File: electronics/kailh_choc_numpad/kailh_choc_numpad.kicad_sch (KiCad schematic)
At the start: 135 parts, among them J1 Conn_01x06, U1 PCA9554, U2 PCA9535

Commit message: updated broken IC footprint, added OHW logo
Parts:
- added N2: OHWLOGO, Symbol:OSHW-Symbol_8.9x8mm_SilkScreen, symbol SquantorLabels:OHWLOGO
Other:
- moved on the sheet: N1
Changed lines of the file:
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@@
     (stroke (width 0) (type default) (color 0 0 0 0))
   )
-  (polyline (pts (xy 175.26 185.42) (xy 157.48 185.42))
+  (polyline (pts (xy 175.26 173.99) (xy 157.48 173.99))
     (stroke (width 0) (type default) (color 0 0 0 0))
   )
@@
     (stroke (width 0) (type default) (color 0 0 0 0))
   )
-  (polyline (pts (xy 157.48 185.42) (xy 157.48 196.85))
+  (polyline (pts (xy 157.48 173.99) (xy 157.48 196.85))
     (stroke (width 0) (type default) (color 0 0 0 0))
   )
@@
     (stroke (width 0) (type default) (color 0 0 0 0))
   )
-  (polyline (pts (xy 175.26 196.85) (xy 175.26 185.42))
+  (polyline (pts (xy 175.26 196.85) (xy 175.26 173.99))
     (stroke (width 0) (type default) (color 0 0 0 0))
   )
@@
     (pin "2")
   )
+  (symbol (lib_id "SquantorLabels:OHWLOGO") (at 166.37 186.69 0) (unit 1)
+    (in_bom yes) (on_board yes)
+    (property "Reference" "N2" (id 0) (at 165.1 182.88 0)
+      (effects (font (size 1.524 1.524)) (justify left))
+    )
+    (property "Value" "OHWLOGO" (id 1) (at 161.29 190.5 0)
+      (effects (font (size 1.524 1.524)) (justify left))
+    )
+    (property "Footprint" "Symbol:OSHW-Symbol_8.9x8mm_SilkScreen" (id 2) (at 166.37 186.69 0)
+      (effects (font (size 1.524 1.524)) hide)
+    )
+    (property "Datasheet" "" (id 3) (at 166.37 186.69 0)
+      (effects (font (size 1.524 1.524)) hide)
+    )
+  )
   (symbol (lib_id "power:VDD") (at 43.18 41.91 270) (unit 1)
     (in_bom yes) (on_board yes)
@@
     )
   )
-  (symbol (lib_id "SquantorLabels:VYYYYMMDD") (at 166.37 190.5 0) (unit 1)
+  (symbol (lib_id "SquantorLabels:VYYYYMMDD") (at 166.37 179.07 0) (unit 1)
     (in_bom yes) (on_board yes)
-    (property "Reference" "N1" (id 0) (at 165.1 187.96 0)
+    (property "Reference" "N1" (id 0) (at 165.1 176.53 0)
       (effects (font (size 1.524 1.524)) (justify left))
     )
-    (property "Value" "V20220626" (id 1) (at 160.02 190.5 0)
+    (property "Value" "V20220626" (id 1) (at 160.02 179.07 0)
       (effects (font (size 1.524 1.524)) (justify left))
     )
-    (property "Footprint" "SquantorLabels:Label_Generic" (id 2) (at 166.37 190.5 0)
+    (property "Footprint" "SquantorLabels:Label_Generic" (id 2) (at 166.37 179.07 0)
       (effects (font (size 1.524 1.524)) hide)
     )
-    (property "Datasheet" "" (id 3) (at 166.37 190.5 0)
+    (property "Datasheet" "" (id 3) (at 166.37 179.07 0)
       (effects (font (size 1.524 1.524)) hide)
     )
@@
       (reference "N1") (unit 1) (value "V20220626") (footprint "SquantorLabels:Label_Generic")
     )
+    (path "/8a622108-1bf1-4789-8ead-8e70429237d1"
+      (reference "N2") (unit 1) (value "OHWLOGO") (footprint "Symbol:OSHW-Symbol_8.9x8mm_SilkScreen")
+    )
     (path "/69128f69-413a-42fa-86a0-bccc9ea098f6"

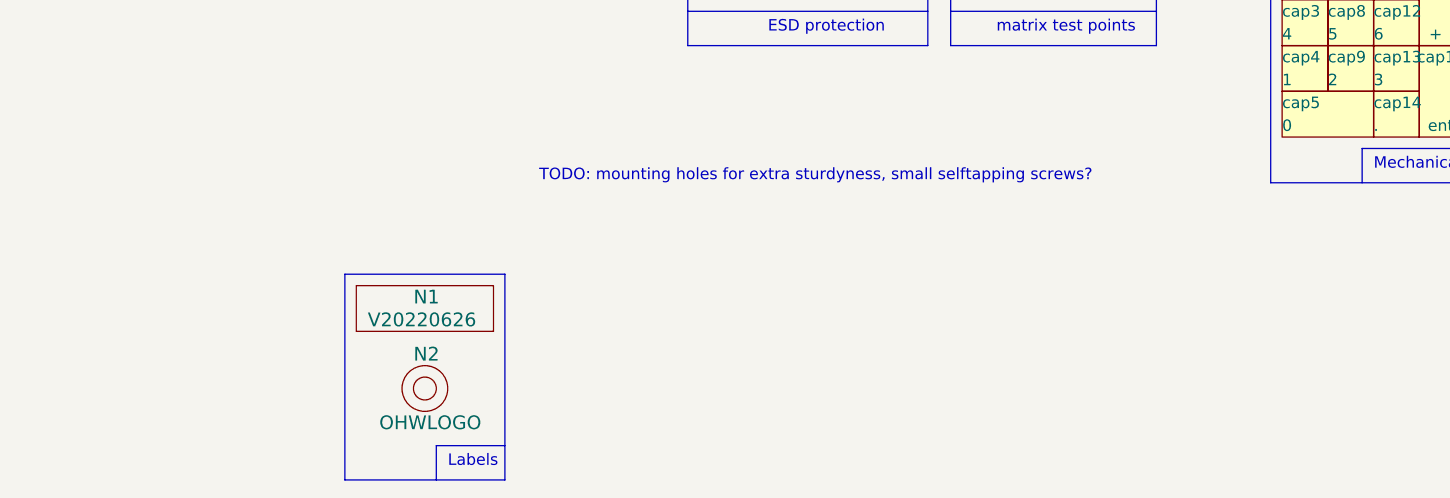
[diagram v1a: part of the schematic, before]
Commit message: added mounting holes
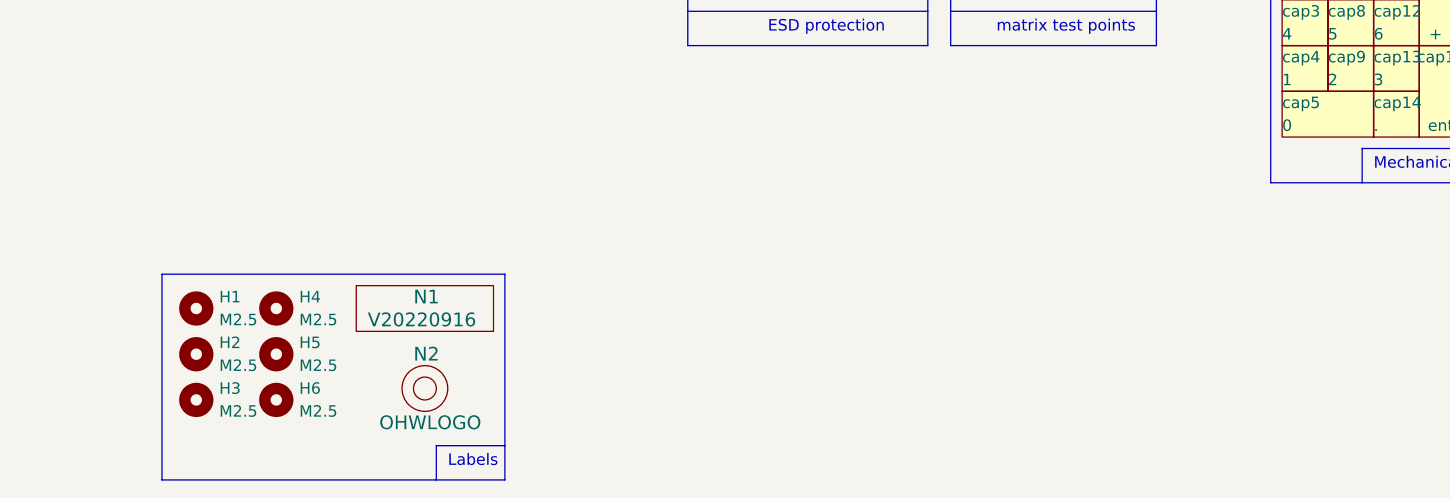
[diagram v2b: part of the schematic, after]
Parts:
- added H1, H2, H3, H4, H5, H6: M2.5, MountingHole:MountingHole_2.7mm_M2.5, symbol Mechanical:MountingHole
- N1: value V20220626 -> V20220916
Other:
- note removed: "TODO: mounting holes for extra sturdyness, small selftapping screws?"
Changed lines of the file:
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@@
     (stroke (width 0) (type default) (color 0 0 0 0))
   )
-  (polyline (pts (xy 175.26 173.99) (xy 157.48 173.99))
+  (polyline (pts (xy 175.26 173.99) (xy 137.16 173.99))
     (stroke (width 0) (type default) (color 0 0 0 0))
   )
@@
     (stroke (width 0) (type default) (color 0 0 0 0))
   )
-  (polyline (pts (xy 157.48 173.99) (xy 157.48 196.85))
+  (polyline (pts (xy 137.16 173.99) (xy 137.16 196.85))
     (stroke (width 0) (type default) (color 0 0 0 0))
   )
@@
     (stroke (width 0) (type default) (color 0 0 0 0))
   )
-  (polyline (pts (xy 157.48 196.85) (xy 175.26 196.85))
+  (polyline (pts (xy 137.16 196.85) (xy 175.26 196.85))
     (stroke (width 0) (type default) (color 0 0 0 0))
   )
@@
     (effects (font (size 1.27 1.27)) (justify left bottom))
   )
-  (text "TODO: mounting holes for extra sturdyness, small selftapping screws?"
-    (at 179.07 163.83 0)
-    (effects (font (size 1.27 1.27)) (justify left bottom))
-  )
   (text "matrix test points" (at 229.87 147.32 0)
     (effects (font (size 1.27 1.27)) (justify left bottom))
@@
     (pin "2")
   )
+  (symbol (lib_id "Mechanical:MountingHole") (at 140.97 177.8 0) (unit 1)
+    (in_bom yes) (on_board yes)
+    (property "Reference" "H1" (id 0) (at 143.51 176.53 0)
+      (effects (font (size 1.27 1.27)) (justify left))
+    )
+    (property "Value" "M2.5" (id 1) (at 143.51 179.07 0)
+      (effects (font (size 1.27 1.27)) (justify left))
+    )
+    (property "Footprint" "MountingHole:MountingHole_2.7mm_M2.5" (id 2) (at 140.97 177.8 0)
+      (effects (font (size 1.27 1.27)) hide)
+    )
+    (property "Datasheet" "~" (id 3) (at 140.97 177.8 0)
+      (effects (font (size 1.27 1.27)) hide)
+    )
+  )
   (symbol (lib_id "Device:D") (at 276.86 20.32 180) (unit 1)
     (in_bom yes) (on_board yes)
@@
     (pin "2")
   )
+  (symbol (lib_id "Mechanical:MountingHole") (at 149.86 182.88 0) (unit 1)
+    (in_bom yes) (on_board yes)
+    (property "Reference" "H5" (id 0) (at 152.4 181.61 0)
+      (effects (font (size 1.27 1.27)) (justify left))
+    )
+    (property "Value" "M2.5" (id 1) (at 152.4 184.15 0)
+      (effects (font (size 1.27 1.27)) (justify left))
+    )
+    (property "Footprint" "MountingHole:MountingHole_2.7mm_M2.5" (id 2) (at 149.86 182.88 0)
+      (effects (font (size 1.27 1.27)) hide)
+    )
+    (property "Datasheet" "~" (id 3) (at 149.86 182.88 0)
+      (effects (font (size 1.27 1.27)) hide)
+    )
+  )
   (symbol (lib_id "Device:R") (at 215.9 25.4 90) (unit 1)
     (in_bom yes) (on_board yes)
@@
     (pin "2")
   )
+  (symbol (lib_id "Mechanical:MountingHole") (at 149.86 187.96 0) (unit 1)
+    (in_bom yes) (on_board yes)
+    (property "Reference" "H6" (id 0) (at 152.4 186.69 0)
+      (effects (font (size 1.27 1.27)) (justify left))
+    )
+    (property "Value" "M2.5" (id 1) (at 152.4 189.23 0)
+      (effects (font (size 1.27 1.27)) (justify left))
+    )
+    (property "Footprint" "MountingHole:MountingHole_2.7mm_M2.5" (id 2) (at 149.86 187.96 0)
+      (effects (font (size 1.27 1.27)) hide)
+    )
+    (property "Datasheet" "~" (id 3) (at 149.86 187.96 0)
+      (effects (font (size 1.27 1.27)) hide)
+    )
+  )
   (symbol (lib_id "power:PWR_FLAG") (at 27.94 189.23 90) (unit 1)
     (in_bom yes) (on_board yes) (fields_autoplaced)
@@
     (pin "2")
   )
+  (symbol (lib_id "Mechanical:MountingHole") (at 140.97 187.96 0) (unit 1)
+    (in_bom yes) (on_board yes)
+    (property "Reference" "H3" (id 0) (at 143.51 186.69 0)
+      (effects (font (size 1.27 1.27)) (justify left))
+    )
+    (property "Value" "M2.5" (id 1) (at 143.51 189.23 0)
+      (effects (font (size 1.27 1.27)) (justify left))
+    )
+    (property "Footprint" "MountingHole:MountingHole_2.7mm_M2.5" (id 2) (at 140.97 187.96 0)
+      (effects (font (size 1.27 1.27)) hide)
+    )
+    (property "Datasheet" "~" (id 3) (at 140.97 187.96 0)
+      (effects (font (size 1.27 1.27)) hide)
+    )
+  )
   (symbol (lib_id "SquantorProto:testpad") (at 231.14 119.38 180) (unit 1)
     (in_bom yes) (on_board yes)
@@
     )
   )
+  (symbol (lib_id "Mechanical:MountingHole") (at 140.97 182.88 0) (unit 1)
+    (in_bom yes) (on_board yes)
+    (property "Reference" "H2" (id 0) (at 143.51 181.61 0)
+      (effects (font (size 1.27 1.27)) (justify left))
+    )
+    (property "Value" "M2.5" (id 1) (at 143.51 184.15 0)
+      (effects (font (size 1.27 1.27)) (justify left))
+    )
+    (property "Footprint" "MountingHole:MountingHole_2.7mm_M2.5" (id 2) (at 140.97 182.88 0)
+      (effects (font (size 1.27 1.27)) hide)
+    )
+    (property "Datasheet" "~" (id 3) (at 140.97 182.88 0)
+      (effects (font (size 1.27 1.27)) hide)
+    )
+  )
   (symbol (lib_id "Device:R") (at 66.04 59.69 90) (unit 1)
     (in_bom yes) (on_board yes)
@@
     (pin "2")
   )
+  (symbol (lib_id "Mechanical:MountingHole") (at 149.86 177.8 0) (unit 1)
+    (in_bom yes) (on_board yes)
+    (property "Reference" "H4" (id 0) (at 152.4 176.53 0)
+      (effects (font (size 1.27 1.27)) (justify left))
+    )
+    (property "Value" "M2.5" (id 1) (at 152.4 179.07 0)
+      (effects (font (size 1.27 1.27)) (justify left))
+    )
+    (property "Footprint" "MountingHole:MountingHole_2.7mm_M2.5" (id 2) (at 149.86 177.8 0)
+      (effects (font (size 1.27 1.27)) hide)
+    )
+    (property "Datasheet" "~" (id 3) (at 149.86 177.8 0)
+      (effects (font (size 1.27 1.27)) hide)
+    )
+  )
   (symbol (lib_id "Device:R") (at 26.67 20.32 90) (unit 1)
     (in_bom yes) (on_board yes)
@@
       (effects (font (size 1.524 1.524)) (justify left))
     )
-    (property "Value" "V20220626" (id 1) (at 160.02 179.07 0)
+    (property "Value" "V20220916" (id 1) (at 160.02 179.07 0)
       (effects (font (size 1.524 1.524)) (justify left))
     )
@@
       (reference "D48") (unit 1) (value "SD05") (footprint "Diode_SMD:D_SOD-323")
     )
+    (path "/0638c28a-738c-40c1-9720-0609b9d04d42"
+      (reference "H1") (unit 1) (value "M2.5") (footprint "MountingHole:MountingHole_2.7mm_M2.5")
+    )
+    (path "/8ca91d34-4828-4d36-b1c6-8447c8b4513c"
+      (reference "H2") (unit 1) (value "M2.5") (footprint "MountingHole:MountingHole_2.7mm_M2.5")
+    )
+    (path "/6ed54721-811a-4d0b-ad81-9f0233492d0e"
+      (reference "H3") (unit 1) (value "M2.5") (footprint "MountingHole:MountingHole_2.7mm_M2.5")
+    )
+    (path "/96163ad0-e355-478e-a87b-8cadde7c0b37"
+      (reference "H4") (unit 1) (value "M2.5") (footprint "MountingHole:MountingHole_2.7mm_M2.5")
+    )
+    (path "/07537a16-dfdd-43a3-8daa-2b692943dfa3"
+      (reference "H5") (unit 1) (value "M2.5") (footprint "MountingHole:MountingHole_2.7mm_M2.5")
+    )
+    (path "/377be5fe-bd95-4b1d-a1fe-9ff5768744f1"
+      (reference "H6") (unit 1) (value "M2.5") (footprint "MountingHole:MountingHole_2.7mm_M2.5")
+    )
     (path "/c9b353ac-f88c-4b2f-962a-c3934916bf5c"
       (reference "J1") (unit 1) (value "Conn_01x06") (footprint "Connector_JST:JST_PH_S6B-PH-K_1x06_P2.00mm_Horizontal")
     )
     (path "/ebe367f5-1f3e-4a04-ac2f-963e9f4d7b90"
-      (reference "N1") (unit 1) (value "V20220626") (footprint "SquantorLabels:Label_Generic")
+      (reference "N1") (unit 1) (value "V20220916") (footprint "SquantorLabels:Label_Generic")
     )
     (path "/8a622108-1bf1-4789-8ead-8e70429237d1"
